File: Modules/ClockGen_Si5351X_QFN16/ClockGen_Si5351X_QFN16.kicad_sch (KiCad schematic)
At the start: 107 parts, among them J1 Screw Terminal, J10 2.54mm Stackable Socket, J11 2.54mm Stackable Socket, J12 2.54mm Stackable Socket, J13 2.54mm Stackable Socket, J14 2.54mm Stackable Socket, J2 JST SH, J3 SMA, J4 2.54 Pins, J5 2.54 Pins, J6 SMA, J7 SMA, J8 SMA, J9 SMA, Q1 GSFJ0300, Q2 GSFK0502, SW1 SW_SPDT, U1 NCV68261, U2 NCV68261, U3 NCP718BSNADJ, U4 SI5351B-B-GM1, U5 AP2127K-ADJ, Y1 25MHz

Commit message: Schematic and PCB progress
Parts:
- added D11: RED, libraries:Worthington_LED_0402, symbol Device:LED_Filled
- added D12: 1N5819W, Diode_SMD:D_SOD-123F, symbol Device:D_Schottky
- added R13: 1k3, libraries:Worthington_R_0201, symbol Device:R_Small_US
- C5: value 1u -> 10u
- R4: value 1k -> 200k
- R5: value 5k83 -> 49k9
- U3: value NCP718BSNADJ -> TPS7E8201; Adjusted Voltage 5.99V -> ~6.010V; Dropout Voltage 380mV -> ~360mV; V_{IN, Max} (none) -> 40V
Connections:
- net +5V: no longer C1.1, J5.2 (Pin_2), J5.4 (Pin_4), Q1.3 (D), U1.3 (D)
- net GND: now also J1.2 (Pin_2), R13.2; no longer J1.1 (Pin_1), J4.1 (Pin_1), J4.3 (Pin_3)
- net VCC: now also C1.1, D4.2 (A), D5.2 (A), Q1.3 (D), R4.2, U1.3 (D), U3.5 (OUT), D12.2 (A); no longer C2.1, J2.2 (Pin_2), Q1.6 (D), U2.3 (D), U3.1 (IN), U3.3 (EN)
- net PWR_IN: now reaches Q1.1 (S), U2.1 (S), U2.4 (EN), U2.6 (IN)
- net PWR_IN: now also J1.1 (Pin_1); no longer J1.2 (Pin_2)
- net +3V3: no longer names the net of Q1.4 (S), U1.1 (S), U1.4 (EN), U1.6 (IN)
- net +3V3: now also J5.2 (Pin_2), J5.4 (Pin_4), D11.1 (K); no longer J4.2 (Pin_2), J4.4 (Pin_4)
- new net: C2.1, D12.1 (K), J2.2 (Pin_2), Q1.6 (D), U2.3 (D), U3.1 (IN), U3.3 (EN)
- new net: D11.2 (A), R13.1
- no-connect marks 0 -> 4
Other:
- note added: "+40V → +5V5 LDO"
- note added: "+9-12V"
- note added: "Allows PCB to survive being placed onto breadboard in either rotation"
- note added: "Reversed Polarity Light"
- note added: "Used to oriente PCB on breadboard"
- note removed: "+24V → +5V LDO"
- note removed: "Used If Powered From 3V3 With 5V Disabled"
- moved on the sheet: C1, J1, J4, J5, Q1B, U1

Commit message: PCB Layout finished
Need to tweak silkscreen and add art and stuff
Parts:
- D12: value 1N5819W -> RB521S-30; footprint Diode_SMD:D_SOD-123F -> Diode_SMD:D_SOD-523; DigiKey 5399-1N5819WCT-ND -> 5399-RB521S-30CT-ND; Part Number 1N5819W -> RB521S-30; V_{F} 0V55 -> 0V50
- R12, R13: value 1k3 -> 1k8
- U4: footprint Package_DFN_QFN:QFN-16-1EP_3x3mm_P0.5mm_EP1.45x1.45mm -> Package_DFN_QFN:QFN-16-1EP_3x3mm_P0.5mm_EP1.9x1.9mm_ThermalVias
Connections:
- net GND: now also SW1.MP
- net VCC: now also D11.2 (A), J2.2 (Pin_2)
- net at J5.2 (Pin_2), J5.4 (Pin_4), Q1.4 (S)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: no longer D11.1 (K)
- net at C2.1, D12.1 (K), Q1.6 (D)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: no longer J2.2 (Pin_2)
- net at R13.1: now also D11.1 (K); no longer D11.2 (A)
- net +3V0 renamed +3V3
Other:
- note removed: "Reversed Polarity Light"
- moved on the sheet: C14, C2, C5, D12, D4, D5, D6, J1, Q1A, R12, R4, R5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

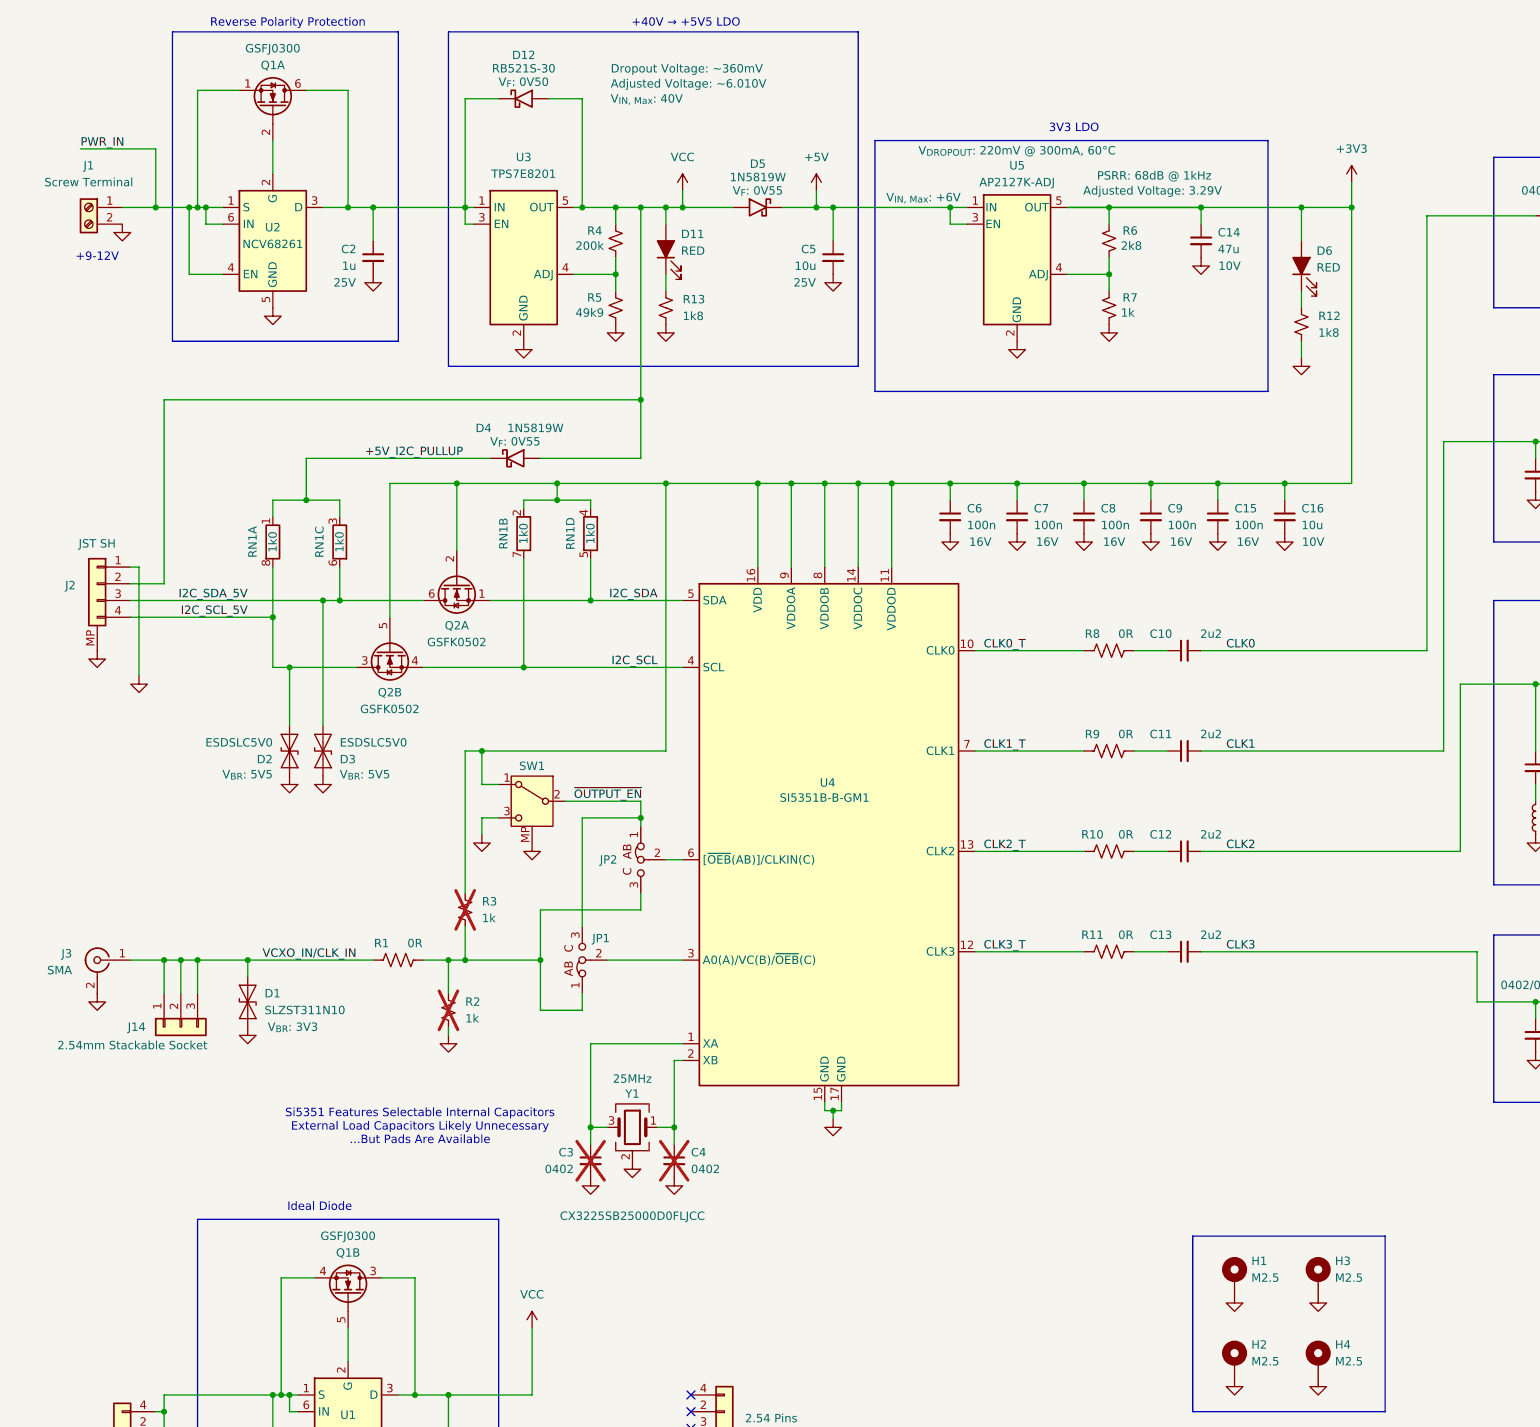
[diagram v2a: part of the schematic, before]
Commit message: Modified designn to include LM66200
PCB layout edits in progress
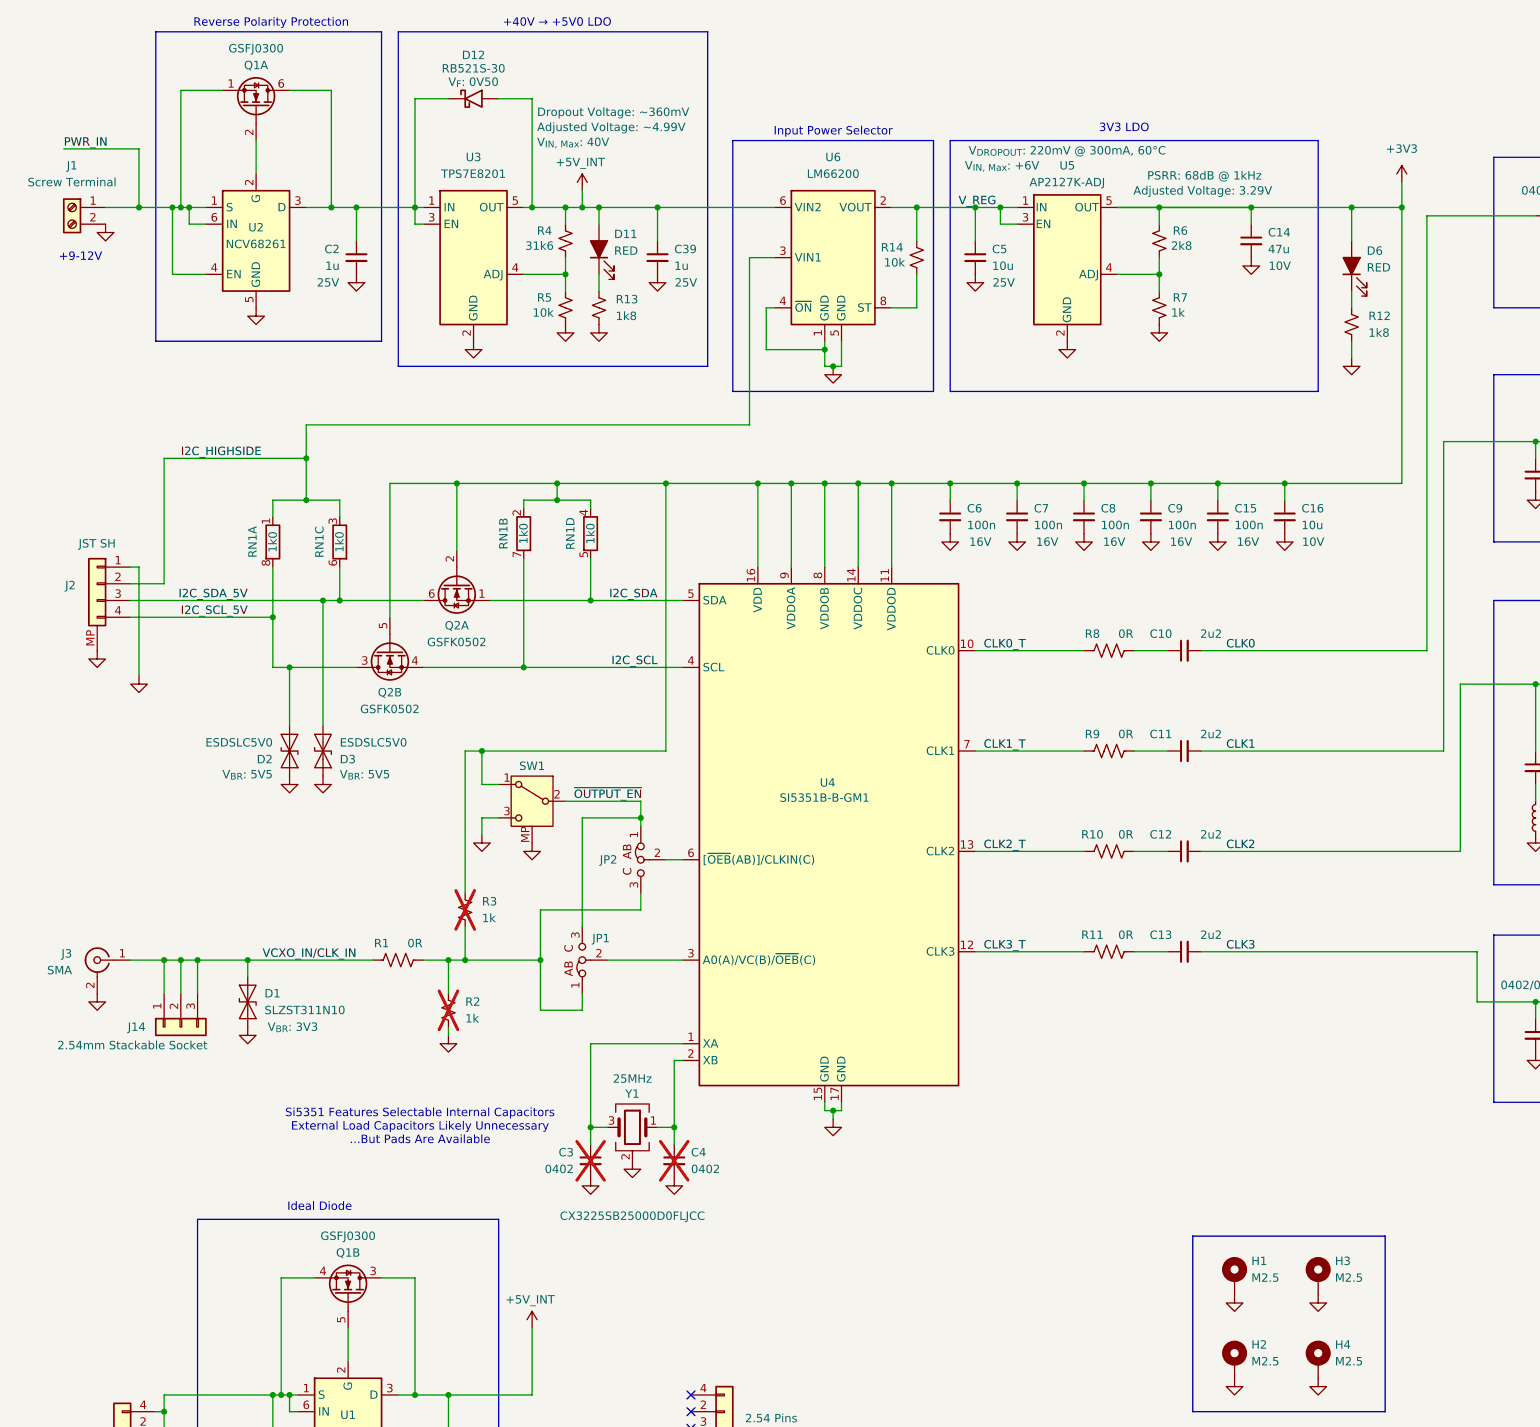
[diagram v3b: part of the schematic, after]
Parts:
- removed D4, D5: 1N5819W, Diode_SMD:D_SOD-123F, symbol Device:D_Schottky
- added C39: 1u, libraries:Worthington_C_0402, symbol Device:C_Small
- added R14: 10k, libraries:Worthington_R_0201, symbol Device:R_Small_US
- added U6: LM66200, Package_TO_SOT_SMD:SOT-583-8, symbol libraries:LM66200
- R4: value 200k -> 31k6
- R5: value 49k9 -> 10k
- U3: Adjusted Voltage ~6.010V -> ~4.99V
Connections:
- net GND: now also C39.2, U6.1 (GND), U6.4 (~{ON}), U6.5 (GND)
- net +5V renamed V_REG
- net V_REG: now also R14.2, U6.2 (VOUT), U6.7 (VOUT)
- net +5V_I2C_PULLUP renamed I2C_HIGHSIDE
- net I2C_HIGHSIDE: now also J2.2 (Pin_2), U6.3 (VIN1)
- net VCC renamed +5V_INT
- net +5V_INT: now also C39.1, U6.6 (VIN2); no longer J2.2 (Pin_2)
- new net: R14.1, U6.8 (ST)
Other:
- note added: "+40V → +5V0 LDO"
- note added: "Input Power Selector"
- note removed: "+40V → +5V5 LDO"
- moved on the sheet: C14, C2, C5, D11, D12, D6, J1, Q1A, R12, R13, R4, R5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

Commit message: PCB Layout
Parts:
- R4, R5, R6, R7: footprint libraries:Worthington_R_0402 -> libraries:Worthington_R_0201
- U1, U2: value NCV68261 -> NCV68061
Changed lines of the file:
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@@
 		)
 	)
-	(netclass_flag ""
-		(length 2.54)
-		(shape round)
-		(at 44.45 166.37 0)
-		(effects
-			(font
-				(size 1.27 1.27)
-			)
-			(justify left bottom)
-		)
-		(property "Net Class" "50R_Coplanar"
-			(at 42.926 164.846 0)
-			(show_name no)
-			(do_not_autoplace no)
-			(effects
-				(font
-					(size 1.27 1.27)
-				)
-				(justify right)
-			)
-		)
-		(property "Component Class" ""
-			(at 78.74 13.97 0)
-			(show_name no)
-			(do_not_autoplace no)
-			(effects
-				(font
-					(size 1.27 1.27)
-					(italic yes)
-				)
-				(justify left)
-			)
-		)
-	)
 	(symbol
 		(lib_id "Switch:SW_SPDT")
@@
 			)
 		)
-		(property "Footprint" "libraries:Worthington_R_0402"
+		(property "Footprint" "libraries:Worthington_R_0201"
 			(at 95.25 57.15 0)
 			(hide yes)
@@
 			)
 		)
-		(property "Footprint" "libraries:Worthington_R_0402"
+		(property "Footprint" "libraries:Worthington_R_0201"
 			(at 185.42 67.31 0)
 			(hide yes)
@@
 			)
 		)
-		(property "Footprint" "libraries:Worthington_R_0402"
+		(property "Footprint" "libraries:Worthington_R_0201"
 			(at 95.25 67.31 0)
 			(hide yes)
@@
 		(in_pos_files yes)
 		(dnp no)
-		(fields_autoplaced yes)
 		(property "Reference" "U1"
-			(at 62.23 235.458 0)
+			(at 62.23 235.966 0)
 			(show_name no)
 			(do_not_autoplace no)
@@
 			)
 		)
-		(property "Value" "NCV68261"
-			(at 62.23 237.998 0)
+		(property "Value" "NCV68061"
+			(at 62.23 238.506 0)
 			(show_name no)
 			(do_not_autoplace no)
@@
 		(in_pos_files yes)
 		(dnp no)
-		(fields_autoplaced yes)
 		(property "Reference" "U2"
-			(at 48.26 55.118 0)
+			(at 48.26 55.626 0)
 			(show_name no)
 			(do_not_autoplace no)
@@
 			)
 		)
-		(property "Value" "NCV68261"
-			(at 48.26 57.658 0)
+		(property "Value" "NCV68061"
+			(at 48.26 58.166 0)
 			(show_name no)
 			(do_not_autoplace no)
@@
 			)
 		)
-		(property "Footprint" "libraries:Worthington_R_0402"
+		(property "Footprint" "libraries:Worthington_R_0201"
 			(at 185.42 57.15 0)
 			(hide yes)

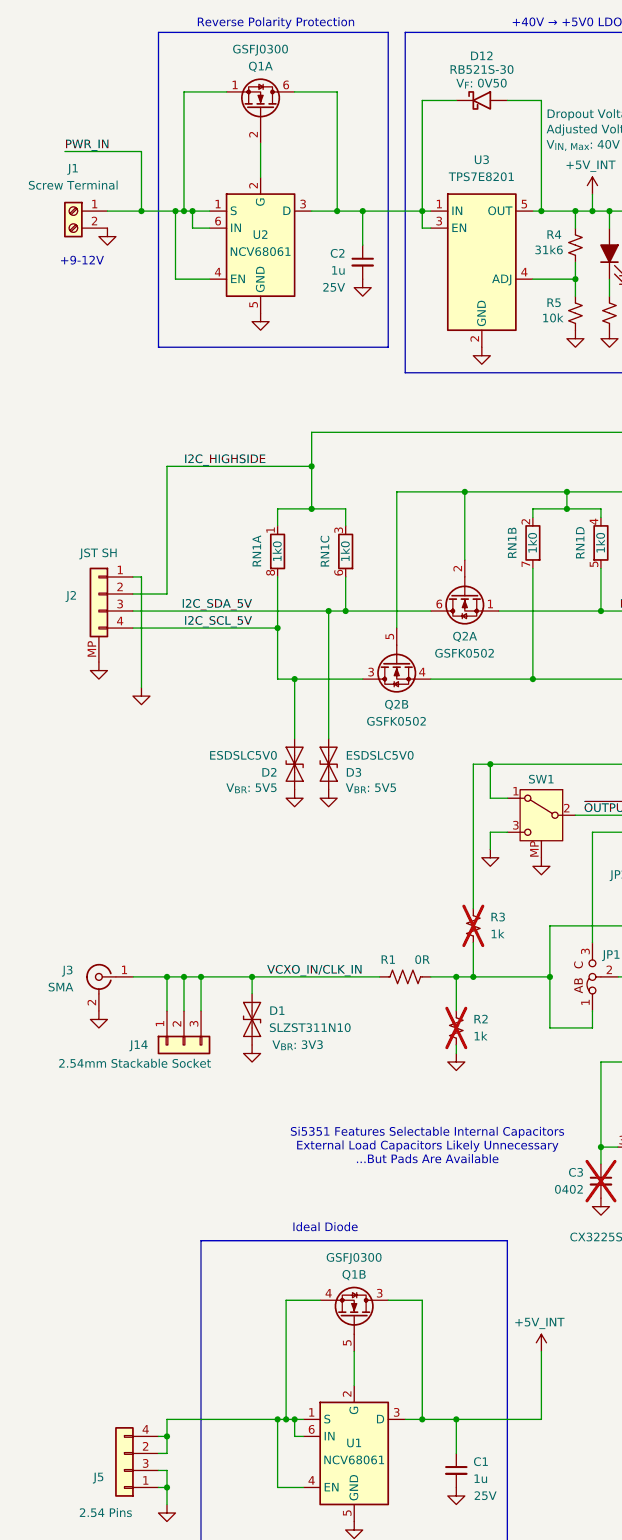
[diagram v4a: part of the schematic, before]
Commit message: Replaced Q2 with GSFJ0300
Lower Rds, smaller footprint, parts commonality with Q1
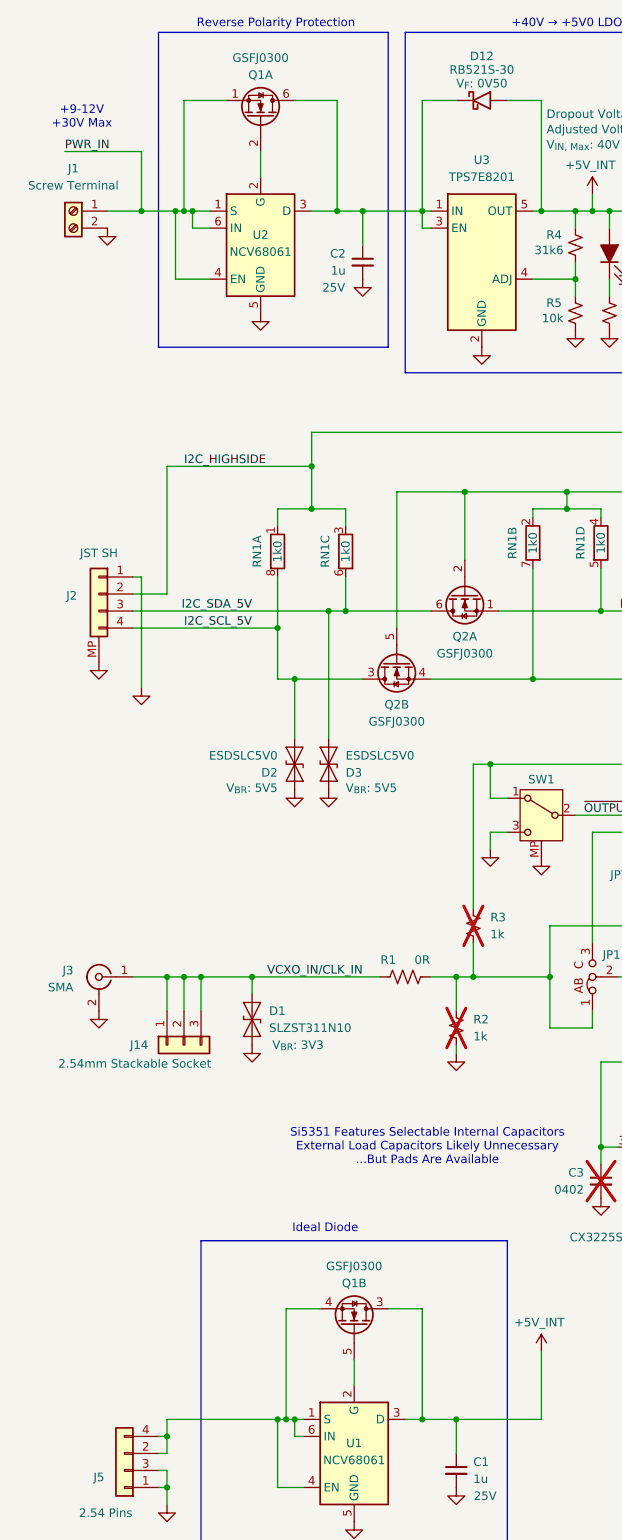
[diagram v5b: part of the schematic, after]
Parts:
- Q2: value GSFK0502 -> GSFJ0300; footprint Package_TO_SOT_SMD:SOT-363_SC-70-6 -> Package_TO_SOT_SMD:SOT-563; DigiKey 4786-GSFK0502CT-ND -> 4786-GSFJ0300CT-ND; Part Number GSFK0502 -> GSFJ0300
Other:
- note added: "+9-12V +30V Max"
- note removed: "+9-12V"
- moved on the sheet: Q1A, Q1B

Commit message: Silkscreen art added
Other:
- note added: "Allows PCB to survive being placed onto breadboard in wrong orientation"
- note added: "Reverse Polarity Protection Reverse Current Protection"
- note removed: "Allows PCB to survive being placed onto breadboard in either rotation"
- note removed: "Ideal Diode"
- note removed: "Reverse Polarity Protection"
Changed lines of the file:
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@@
 		)
 	)
-	(text "Reverse Polarity Protection"
+	(text "Reverse Polarity Protection\nReverse Current Protection"
 		(exclude_from_sim no)
-		(at 50.546 24.13 0)
+		(at 50.546 22.86 0)
 		(effects
 			(font
@@
 		)
 	)
-	(text "Ideal Diode"
-		(exclude_from_sim no)
-		(at 57.912 203.962 0)
-		(effects
-			(font
-				(size 1.27 1.27)
-			)
-		)
-	)
-	(text "Allows PCB to survive being placed\nonto breadboard in either rotation"
+	(text "Allows PCB to survive being placed\nonto breadboard in wrong orientation"
 		(exclude_from_sim no)
 		(at 60.96 259.588 0)
@@
 		(effects
 			(font
+				(size 1.27 1.27)
+			)
+		)
+	)
+	(text "Reverse Polarity Protection\nReverse Current Protection"
+		(exclude_from_sim no)
+		(at 62.23 202.946 0)
+		(effects
+			(font

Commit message: Fixed NCV68601 Footprint
Had the wrong pinout, glad I caught this!
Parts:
- C1, C10, C11, C12, C13, C16, C2, C3, C39, C4, C5: footprint libraries:Worthington_C_0402 -> libraries:Worthington_C_Narrow_0402
- C15, C6, C7, C8, C9: footprint libraries:Worthington_C_0201 -> libraries:Worthington_C_Narrow_0201
- C17, C18, C19, C20, C21, C22, C23, C24, C25, C26, C27, C28, C29, C30, C31, C32, C33, C34, C35, C36, C37, C38: footprint libraries:Worthington_C_0402_0603 -> libraries:Worthington_C_Narrow_0402_0603
- L1, L10, L11, L12, L13, L14, L15, L16, L2, L3, L4, L5, L6, L7, L8, L9: footprint libraries:Worthington_L_0603_RF -> libraries:Worthington_L_Narrow_0603_RF
- R1, R10, R11, R2, R3, R8, R9: footprint libraries:Worthington_R_0402 -> libraries:Worthington_R_Narrow_0402
- R12, R13, R14, R4, R5, R6, R7: footprint libraries:Worthington_R_0201 -> libraries:Worthington_R_Narrow_0201
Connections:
- net +5V_INT: now also U1.4 (D); no longer U1.3 (D)
- net GND: now also U1.2 (GND), U2.2 (GND); no longer U1.5 (GND), U2.5 (GND)
- net PWR_IN: now also U2.3 (EN); no longer U2.4 (EN)
- net at J5.2 (Pin_2), J5.4 (Pin_4), Q1.4 (S)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: now also U1.3 (EN); no longer U1.4 (EN)
- net at Q1.5 (G): now also U1.5 (G); no longer U1.2 (G)
- net at C2.1, D12.1 (K), Q1.6 (D)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: now also U2.4 (D); no longer U2.3 (D)
- net at Q1.2 (G): now also U2.5 (G); no longer U2.2 (G)
